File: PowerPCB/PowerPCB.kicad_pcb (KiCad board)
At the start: 2 copper layers, 60 parts, among them J1 Conn_01x03_Male, J2 Conn_01x10_Male, J3 Conn_01x07_Male, K1 1721081-5, K2 1721081-5, K3 1721081-5, Q1 Q_PMOS_DGS, U1 NCP1117-5.0_SOT223, U2 NCP1117-3.3_SOT223, U3 MCP2562-E-P, U4 MCP2562-E-P, U5 STM32F413ZHTx

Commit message: organizing PCB layout
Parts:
- moved D9 114.6 mm to (335.8, 232.8), turned to 90 degrees
- moved D11 107.4 mm to (340.4, 218.8), turned to 180 degrees
- moved D10 98.9 mm to (345.2, 221.4)
- moved R21 97.3 mm to (345.0, 216.4), turned to 180 degrees
- moved D8 94.4 mm to (341.8, 232.9), turned to 270 degrees
- moved R22 92.1 mm to (351.4, 221.2), turned to 180 degrees
- moved C15 90.4 mm to (351.2, 216.6), turned to 180 degrees
- moved R20 89.3 mm to (347.4, 228.8), turned to 270 degrees
- moved D6 87.4 mm to (375.1, 190.8), turned to 180 degrees
- moved R17 86.5 mm to (370.8, 191.6), turned to 180 degrees
- moved R19 84.2 mm to (347.4, 233.4), turned to 270 degrees
- moved R18 79.9 mm to (370.8, 196.4)
- moved C14 79.9 mm to (352.4, 228.8), turned to 270 degrees
- moved D7 75.9 mm to (375.1, 196.4)
- moved C13 75.3 mm to (370.8, 200.0)
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
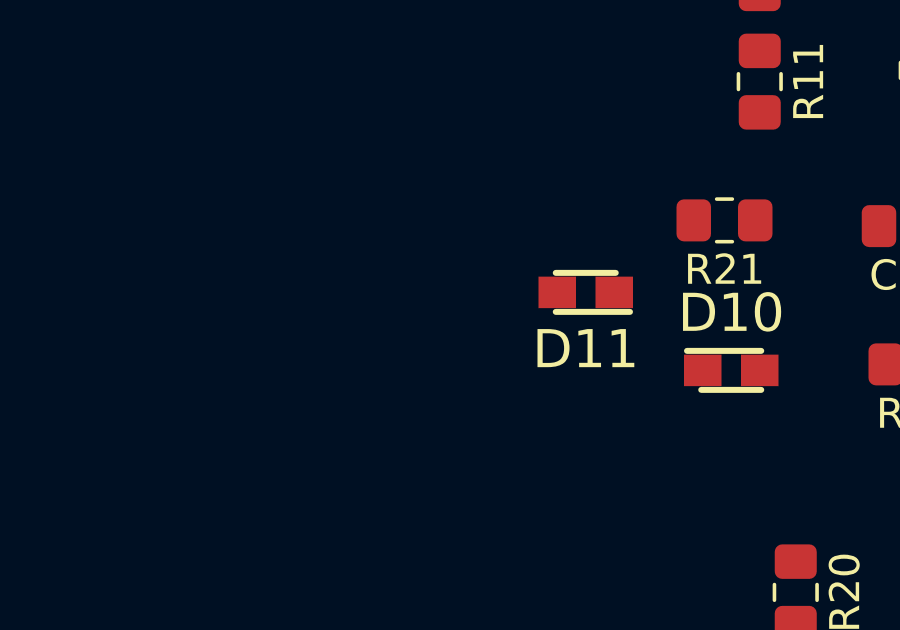
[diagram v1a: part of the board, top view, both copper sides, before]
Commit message: text changes and organization PCB
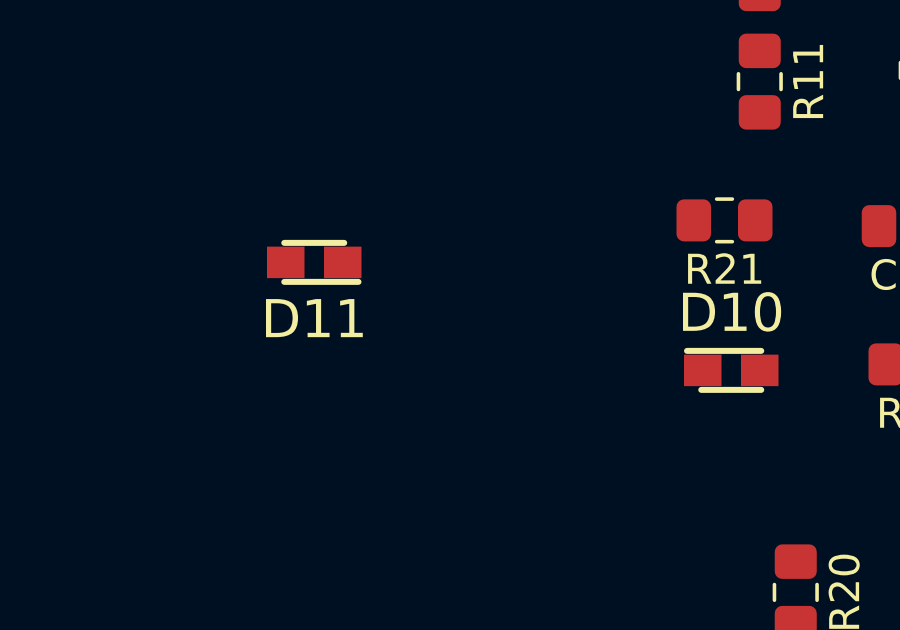
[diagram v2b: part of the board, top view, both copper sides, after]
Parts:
- moved D11 9.11 mm to (331.4, 217.8)
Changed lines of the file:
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@@
   )
   (module SamacSys_Parts:DIOM2013X100N (layer F.Cu)
-    (at 340.4 218.8 180)
+    (at 331.35 217.8 180)
     (descr 0805)
     (tags "Schottky Diode")

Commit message: edge cut
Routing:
- net /Fan/FanPWM: track 0.00 -> 113.3 mm
- net /Fan/FanCtrl: track 0.00 -> 98.6 mm
- net Net-(J2-Pad10): track 0.00 -> 85.8 mm
- net VCC_12: track 0.00 -> 84.5 mm
- net Net-(J2-Pad8): track 0.00 -> 83.2 mm
- net Net-(J2-Pad9): track 0.00 -> 79.8 mm
- net DCDC_ON: track 0.00 -> 57.9 mm
- net AUX+: track 0.00 -> 7.27 mm
- net (no net): vias 0 -> 2
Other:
- board outline added: 257 x 199.8 mm

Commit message: Finished Layout of parts on PCB
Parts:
- moved J3 66.0 mm to (403.6, 160.4)
- moved Q1 47.5 mm to (350.2, 174.0)
- moved R16 47.5 mm to (350.2, 168.6)
- moved J2 41.8 mm to (341.4, 195.6)
- moved R9 39.3 mm to (406.2, 222.6)
- moved D1 39.3 mm to (410.2, 222.6)
- moved D3 34.9 mm to (410.2, 216.8)
- moved D4 34.7 mm to (410.2, 193.8)
- moved R14 34.7 mm to (406.2, 193.8)
- moved D2 34.7 mm to (410.2, 187.8)
- moved D5 34.7 mm to (410.2, 182.8)
- moved R12 34.7 mm to (406.2, 187.8)
- moved R15 34.7 mm to (406.2, 182.8)
- moved R13 34.3 mm to (406.2, 216.8)
- moved J1 32.7 mm to (403.6, 204.4)
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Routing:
- net /Fan/FanPWM: track 113.3 -> 0.00 mm
- net /Fan/FanCtrl: track 98.6 -> 0.00 mm
- net Net-(J2-Pad10): track 85.8 -> 0.00 mm
- net VCC_12: track 84.5 -> 0.00 mm
- net Net-(J2-Pad8): track 83.2 -> 0.00 mm
- net Net-(J2-Pad9): track 79.8 -> 0.00 mm
- net DCDC_ON: track 57.9 -> 0.00 mm
- net AUX+: track 7.27 -> 0.00 mm
- net (no net): vias 2 -> 0
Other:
- board outline removed

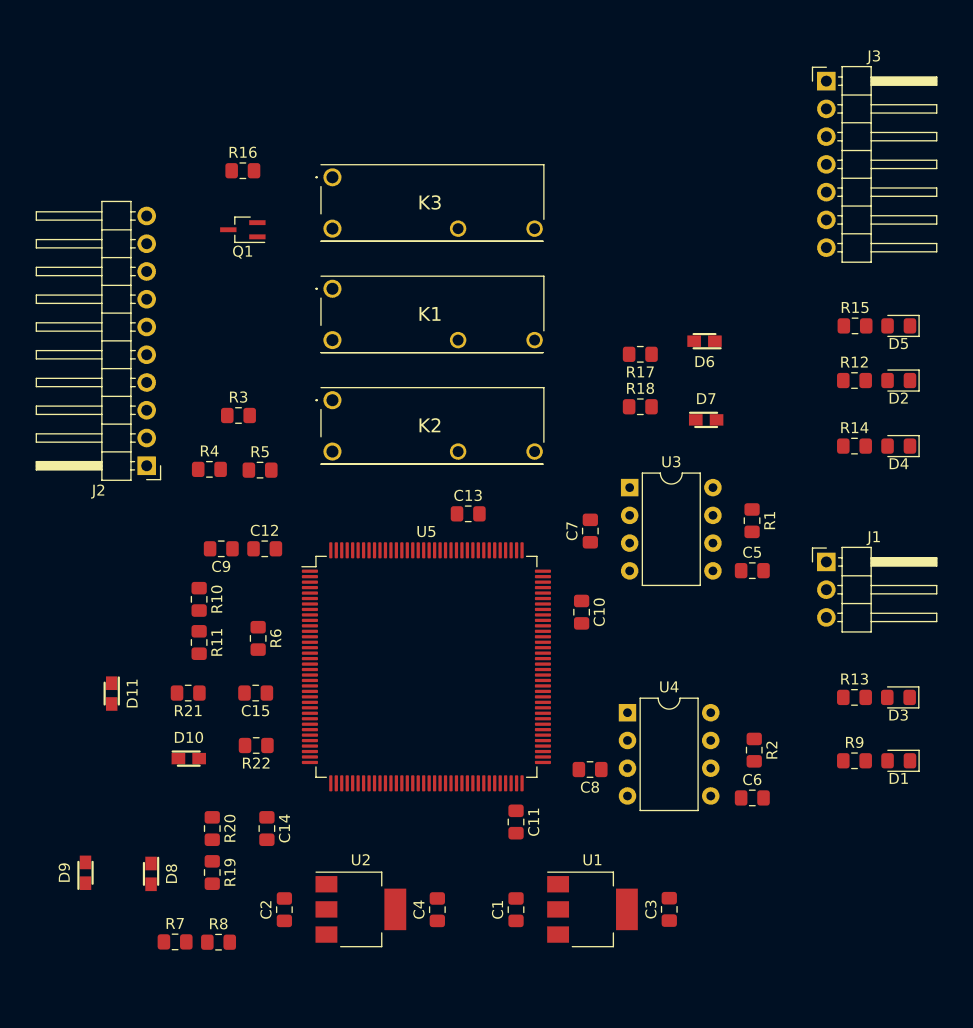
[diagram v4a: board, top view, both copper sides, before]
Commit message: tracks and ground plane draft 1 done
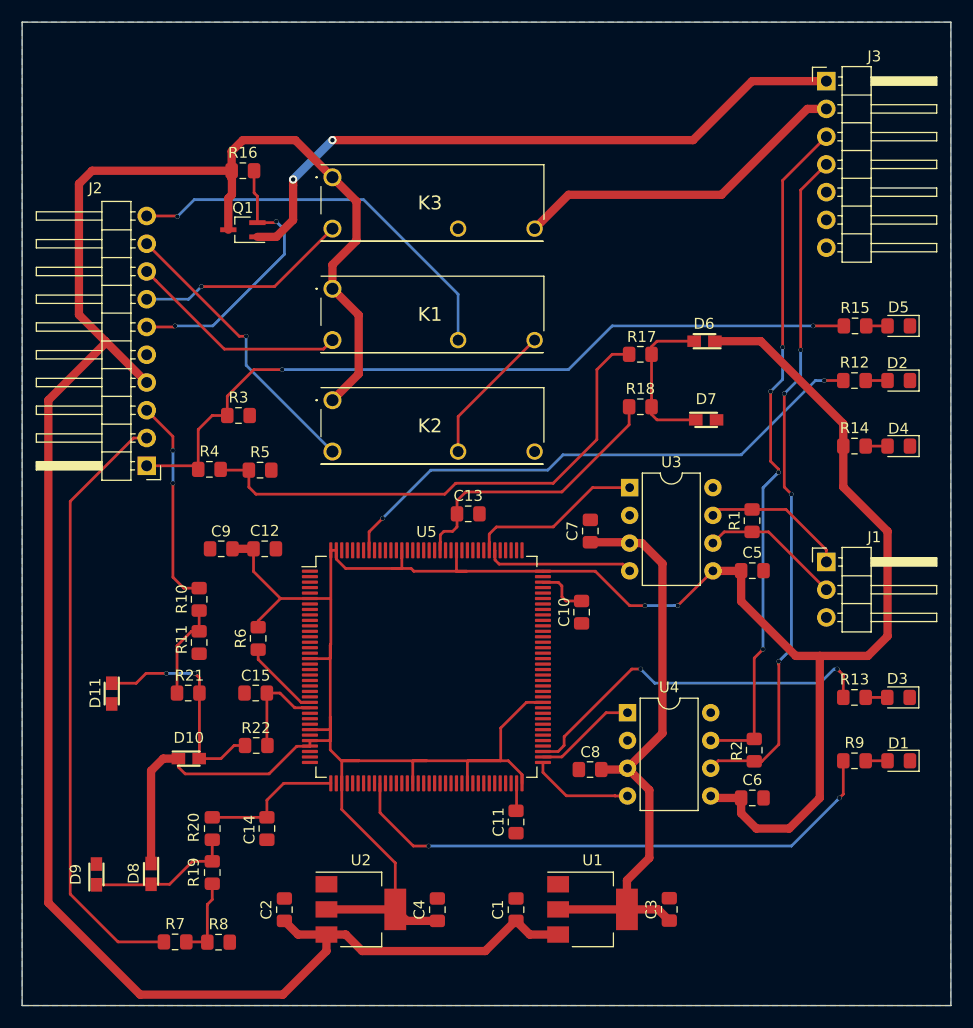
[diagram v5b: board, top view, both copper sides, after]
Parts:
- moved D9 1.01 mm to (336.8, 233.0)
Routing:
- net VCC_3.3: track 0.00 -> 259.9 mm, vias 0 -> 2
- net VCC_12: track 0.00 -> 191.3 mm
- net DCDC_ON: track 0.00 -> 72.6 mm, vias 0 -> 2
- net MAIN_CAN_LO: track 0.00 -> 62.6 mm, vias 0 -> 4
- net MAIN_CAN_HI: track 0.00 -> 62.5 mm, vias 0 -> 4
- net /Fan/Fan+: track 0.00 -> 60.1 mm, vias 0 -> 2
- net AUX+: track 0.00 -> 55.7 mm
- net VCC_5: track 0.00 -> 55.1 mm
- net Net-(R9-Pad1): track 0.00 -> 51.4 mm, vias 0 -> 2
- net Net-(R12-Pad1): track 0.00 -> 50.8 mm, vias 0 -> 2
- net /InputProtection/Vin: track 0.00 -> 48.3 mm
- net Net-(J2-Pad10): track 0.00 -> 36.9 mm, vias 0 -> 1
- net Net-(R13-Pad1): track 0.00 -> 34.4 mm, vias 0 -> 2
- net /Fan/Fan-: track 0.00 -> 31.2 mm
- net Net-(J2-Pad9): track 0.00 -> 26.4 mm, vias 0 -> 1
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- added copper zone on B.Cu, net GND
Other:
- board outline added: 85 x 90 mm
- net class Default: trace_width 0.762 -> 0.254; via_dia 0.8 -> 0.4064

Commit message: moved pcb to middle of page
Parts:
- added C13: 100n, Capacitor_SMD:C_0805_2012Metric_Pad1.15x1.40mm_HandSolder, F.Cu at (189.0, 117.8)
- added C14: 100n, Capacitor_SMD:C_0805_2012Metric_Pad1.15x1.40mm_HandSolder, F.Cu at (189.0, 120.7)
- added C15: 100n, Capacitor_SMD:C_0805_2012Metric_Pad1.15x1.40mm_HandSolder, F.Cu at (193.8, 117.8)
- added C16: 100n, Capacitor_SMD:C_0805_2012Metric_Pad1.15x1.40mm_HandSolder, F.Cu at (189.0, 123.7)
- added C17: 100n, Capacitor_SMD:C_0805_2012Metric_Pad1.15x1.40mm_HandSolder, F.Cu at (193.8, 120.7)
- added C18: 100n, Capacitor_SMD:C_0805_2012Metric_Pad1.15x1.40mm_HandSolder, F.Cu at (198.5, 117.8)
- added C19: 100n, Capacitor_SMD:C_0805_2012Metric_Pad1.15x1.40mm_HandSolder, F.Cu at (193.8, 123.7)
- added C20: 100n, Capacitor_SMD:C_0805_2012Metric_Pad1.15x1.40mm_HandSolder, F.Cu at (198.5, 120.7)
- added C21: 100n, Capacitor_SMD:C_0805_2012Metric_Pad1.15x1.40mm_HandSolder, F.Cu at (203.2, 117.8)
- added C22: 4.7u, Capacitor_SMD:C_0805_2012Metric_Pad1.15x1.40mm_HandSolder, F.Cu at (198.5, 123.7)
- added C23: 100n, Capacitor_SMD:C_0805_2012Metric_Pad1.15x1.40mm_HandSolder, F.Cu at (203.2, 120.7)
- C12: renamed from C9; value C -> 100n
- C24: renamed from C13; value 10u -> 0.01u
- C25: renamed from C14; value 10u -> 0.01u
- C26: renamed from C15; value 10u -> 0.01u
- R12, R13, R14, R15, R9: value R -> 100
- moved C1 260.9 mm to (137.9, 127.7)
- moved C10 260.9 mm to (137.9, 119.7)
- moved C11 260.9 mm to (115.0, 94.7)
- moved C12 260.9 mm to (111.0, 94.7)
- moved C2 260.9 mm to (116.8, 127.7)
- moved C24 260.9 mm to (133.6, 91.5)
- moved C26 260.9 mm to (114.1, 107.9)
- moved C3 260.9 mm to (152.0, 127.7)
- moved C4 260.9 mm to (130.8, 127.7)
- moved C5 260.9 mm to (159.6, 96.7)
- moved C6 260.9 mm to (159.6, 117.5)
- moved C7 260.9 mm to (144.8, 93.1)
- moved C8 260.9 mm to (144.7, 114.9)
- moved C9 260.9 mm to (143.9, 100.5)
- moved D1 260.9 mm to (173.0, 114.1)
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- renumbered C11 to C10, C12 to C11, C10 to C9
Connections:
- U5 pad 95: Net-(U5-Pad95) -> VCC_3.3
